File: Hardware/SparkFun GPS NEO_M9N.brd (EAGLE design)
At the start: 40.6 x 33.3 mm, 93 parts, among them J13 U.FL, J2 Qwiic Right Angle, J4 Qwiic Right Angle, U1 U-BLOX_NEO-M9N, U2 3.3V

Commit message: Initial issues dealt with, air wires etc
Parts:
- removed U$27: (no value), buzzard_labels (6):DSEL0
- removed U$32: (no value), buzzard_labels (5):JP32
- removed U$53: (no value), buzzard_labels (7):NEO#M8P3
- removed U$54: (no value), buzzard_labels (8):GPS#RTK1
- moved JP2 3.02 mm to (35.1, 11.9)
- moved JP1 1.90 mm to (35.1, 9.60)
- moved U$12 0.66 mm to (40.0, 9.50)
- moved D3 0.64 mm to (10.1, 24.4)
- moved U$25 0.54 mm to (39.8, 11.9)
- moved R8 0.53 mm to (4.09, 22.3)
- moved R9 0.41 mm to (9.55, 21.9)
- moved R10 0.36 mm to (11.4, 22.0)
- moved J3 0.33 mm to (10.1, 26.8)
- moved R7 0.31 mm to (2.59, 22.3)
- moved R12 0.30 mm to (7.52, 23.1)
- moved J2 0.28 mm to (5.08, 16.2)
- moved J4 0.28 mm to (35.6, 16.2)
- moved JP31 0.28 mm to (2.54, 30.5)
- moved JP41 0.28 mm to (38.1, 30.5)
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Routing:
- net 3.3V: track 115.8 -> 109.2 mm, vias 8 -> 7
- net N$1: track 0.00 -> 5.81 mm, vias 0 -> 1
- net N$5: track 0.67 -> 4.61 mm, vias 0 -> 1
- net N$8: track 0.67 -> 4.11 mm, vias 0 -> 1
- net N$12: track 52.7 -> 53.5 mm
- net GND: track 1.72 -> 2.56 mm, vias 159 -> 169
- net PPS: track 37.6 -> 36.8 mm
- net 5V: track 61.5 -> 60.7 mm
- net N$4: track 5.26 -> 5.88 mm
- net N$11: track 55.1 -> 55.6 mm
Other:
- board size 40.6 x 33.3 mm -> 40.6 x 33 mm

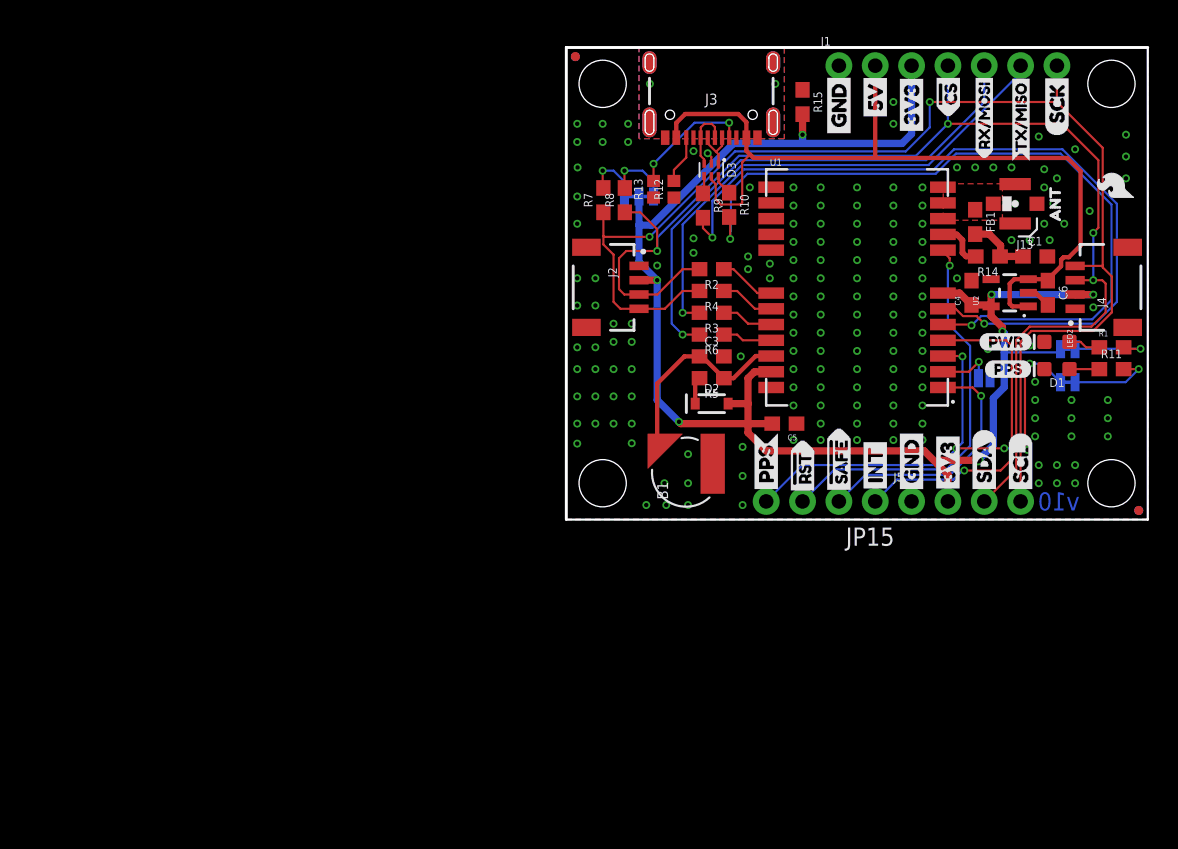
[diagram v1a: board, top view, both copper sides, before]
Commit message: Updates the order of the info boxes in the schematic, adds 10k pullup to D_SEL
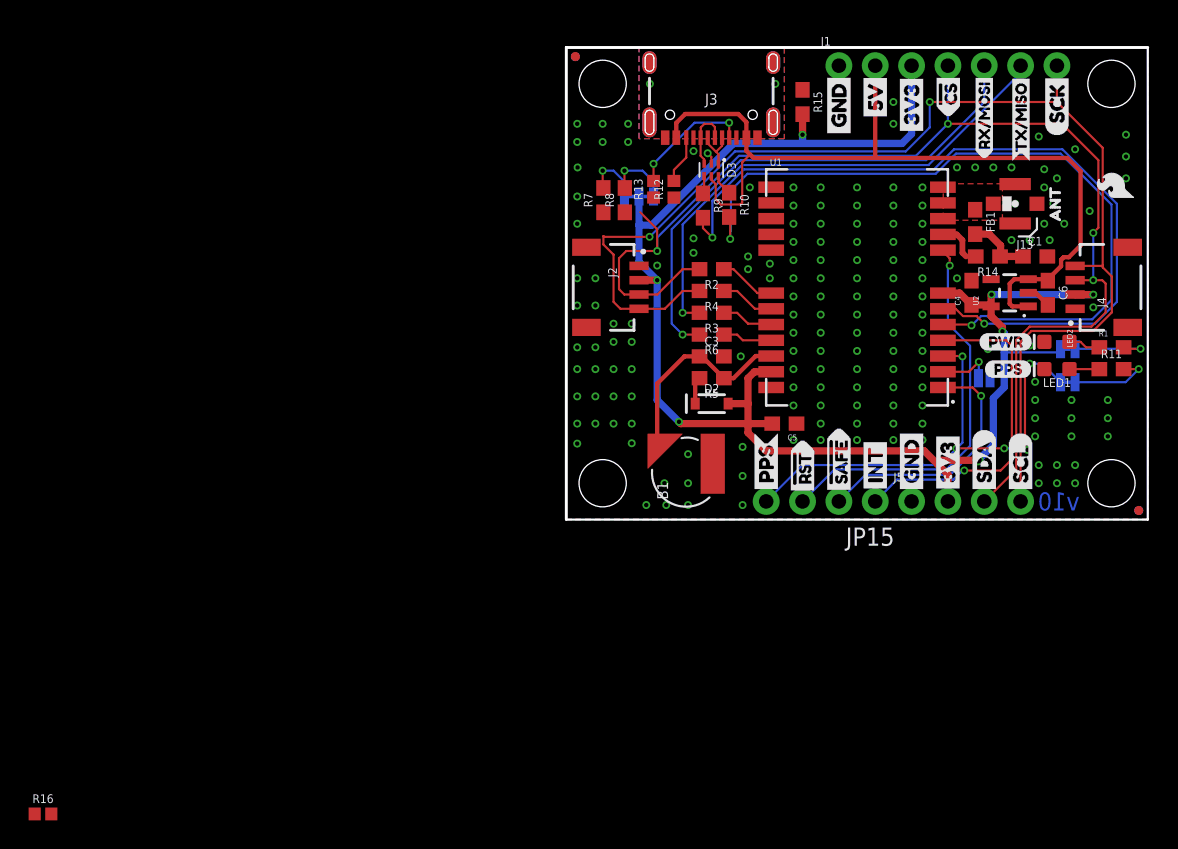
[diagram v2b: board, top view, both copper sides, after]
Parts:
- added R16: 10k, SparkFun-Resistors:0402
- moved LOGO2 6.28 mm to (20.2, 20.7)
- moved U$22 0.92 mm to (24.5, 18.4)
- renumbered D1 to LED1
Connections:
- net N$13 renamed VCC_RF
- net 3.3V: now also R16.2
- net D_SEL: now also R16.1
- net SCL/SCK: now also R8.1; no longer R7.1
- net SDA/!CS: now also R7.1; no longer R8.1
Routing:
- net SCL/SCK: track 89.1 -> 87.4 mm
- net SDA/!CS: track 88.0 -> 87.0 mm
- net VCC_RF: track 3.45 -> 2.78 mm
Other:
- board text added: "Elias Santistevan"
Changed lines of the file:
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@@
 <dimension x1="2.54" y1="2.54" x2="2.54" y2="30.48" x3="-2.54" y3="16.51" textsize="1.778" textratio="15" layer="47" unit="inch"/>
 <dimension x1="2.54" y1="30.48" x2="38.1" y2="30.48" x3="20.32" y3="45.72" textsize="1.778" textratio="15" layer="47" unit="inch"/>
+<text x="12.7" y="-17.78" size="1.778" layer="51" font="vector">Elias Santistevan</text>
 </plain>
 <attributes>
@@
 <attribute name="VALUE" x="5.08" y="21.4376" size="0.6096" layer="28" font="vector" ratio="20" rot="MR0" align="top-center"/>
 </element>
-<element name="D1" library="SparkFun-LED" package="LED-0603" value="Yellow" x="34.29" y="10.5156" smashed="yes" rot="R180">
+<element name="LED1" library="SparkFun-LED" package="LED-0603" value="Yellow" x="34.29" y="10.5156" smashed="yes" rot="R180">
 <attribute name="NAME" x="34.29" y="9.8806" size="0.6096" layer="25" font="vector" ratio="20" rot="R180" align="bottom-center"/>
 <attribute name="PROD_ID" value="DIO-09003" x="34.29" y="10.5156" size="1.778" layer="27" rot="R180" display="off"/>
@@
 <element name="U$15" library="buzzard_labels (5)" package="INT8" value="" x="21.59" y="1.651" smashed="yes" rot="R90"/>
 <element name="U$16" library="buzzard_labels (5)" package="INT8" value="" x="21.59" y="1.651" smashed="yes" rot="MR90"/>
-<element name="U$22" library="buzzard_labels (5)" package="U#BLOX3" value="" x="25.273" y="17.8816" smashed="yes" rot="MR0"/>
+<element name="U$22" library="buzzard_labels (5)" package="U#BLOX3" value="" x="24.511" y="18.3896" smashed="yes" rot="MR0"/>
 <element name="U$30" library="Labels" package="QWIIC-LOGO-MEDIUM" value="" x="4.191" y="8.4836" smashed="yes" rot="MR0"/>
 <element name="U$35" library="buzzard_labels (7)" package="#RST3" value="" x="16.51" y="1.397" smashed="yes" rot="R90"/>
@@
 <element name="U$34" library="buzzard_labels (36)" package="TX#MISO0" value="" x="31.7754" y="24.9936" smashed="yes" rot="R90"/>
 <element name="U$37" library="buzzard_labels (36)" package="TX#MISO1" value="" x="31.7754" y="24.0284" smashed="yes" rot="MR90"/>
-<element name="LOGO2" library="SparkFun-Aesthetics" package="SFE_LOGO_NAME_FLAME_.1" value="SFE_LOGO_NAME_FLAME.1_INCH" x="26.289" y="19.1516" smashed="yes" rot="MR0"/>
+<element name="LOGO2" library="SparkFun-Aesthetics" package="SFE_LOGO_NAME_FLAME_.1" value="SFE_LOGO_NAME_FLAME.1_INCH" x="20.193" y="20.6756" smashed="yes" rot="MR0"/>
 <element name="U1" library="gps" package="NEO-M9N" value="U-BLOX_NEO-M9N" x="20.32" y="16.2306" smashed="yes">
 <attribute name="NAME" x="14.22" y="24.7306" size="0.508" layer="25"/>
@@
 <attribute name="PROD_ID" value="RES-14340" x="6.096" y="23.0886" size="1.778" layer="27" font="vector" ratio="15" rot="R90" display="off"/>
 <attribute name="VALUE" x="6.858" y="23.0886" size="0.6096" layer="27" font="vector" ratio="20" rot="R90" align="top-center"/>
+</element>
+<element name="R16" library="SparkFun-Resistors" package="0402" value="10k" x="-36.576" y="-20.574" smashed="yes">
+<attribute name="NAME" x="-36.576" y="-19.812" size="0.6096" layer="25" font="vector" ratio="20" align="bottom-center"/>
+<attribute name="PROD_ID" value="RES-14241" x="-36.576" y="-20.574" size="1.778" layer="27" font="vector" display="off"/>
+<attribute name="VALUE" x="-36.576" y="-21.336" size="0.6096" layer="27" font="vector" ratio="20" align="top-center"/>
 </element>
 </elements>
@@
 <wire x1="5.97123125" y1="20.574" x2="5.08" y2="20.574" width="0.508" layer="16"/>
 <wire x1="11.68623125" y1="26.289" x2="5.97123125" y2="20.574" width="0.508" layer="16"/>
+<contactref element="R16" pad="2"/>
+<wire x1="6.35" y1="8.3566" x2="-35.996" y2="-20.574" width="0" layer="19" extent="1-16"/>
 </signal>
 <signal name="GND">
@@
 <contactref element="C3" pad="2"/>
 <contactref element="B1" pad="-"/>
-<contactref element="D1" pad="C"/>
+<contactref element="LED1" pad="C"/>
 <polygon width="0.1524" layer="1" isolate="0.2032" rank="4">
 <vertex x="0" y="32.9946"/>
@@
 <contactref element="J2" pad="4"/>
 <contactref element="J4" pad="4"/>
-<contactref element="R7" pad="1"/>
 <contactref element="R4" pad="2"/>
 <wire x1="5.08" y1="14.7306" x2="6.882" y2="14.7306" width="0.1524" layer="1"/>
@@
 <via x="5.8180875" y="19.7612" extent="1-16" drill="0.3048"/>
 <wire x1="2.5908" y1="19.2278" x2="3.302" y2="18.5166" width="0.1524" layer="1"/>
-<wire x1="2.5908" y1="21.4766" x2="2.5908" y2="19.812" width="0.1524" layer="1"/>
 <wire x1="2.5908" y1="19.812" x2="2.5908" y2="19.2278" width="0.1524" layer="1"/>
 <wire x1="5.8180875" y1="19.7612" x2="2.6416" y2="19.7612" width="0.1524" layer="1"/>
 <wire x1="2.6416" y1="19.7612" x2="2.5908" y2="19.812" width="0.1524" layer="1"/>
+<contactref element="R8" pad="1"/>
+<wire x1="2.6416" y1="19.7612" x2="4.0894" y2="21.4766" width="0" layer="19" extent="1-1"/>
 </signal>
 <signal name="SDA/!CS">
 <contactref element="J2" pad="3"/>
 <contactref element="J4" pad="3"/>
-<contactref element="R8" pad="1"/>
 <contactref element="R2" pad="2"/>
 <wire x1="6.358" y1="15.7306" x2="8.128" y2="17.5006" width="0.1524" layer="1"/>
@@
 <contactref element="J5" pad="3"/>
 <wire x1="31.4452" y1="3.5052" x2="29.21" y2="1.27" width="0.1524" layer="1"/>
-<wire x1="4.0894" y1="21.4766" x2="5.168" y2="21.4766" width="0.1524" layer="1"/>
 <wire x1="5.168" y1="21.4766" x2="6.35" y2="20.2946" width="0.1524" layer="1"/>
 <wire x1="6.35" y1="20.2946" x2="6.35" y2="18.7706" width="0.1524" layer="1"/>
@@
 <wire x1="4.056" y1="15.7306" x2="3.683" y2="16.1036" width="0.1524" layer="1"/>
 <wire x1="5.08" y1="15.7306" x2="6.358" y2="15.7306" width="0.1524" layer="1"/>
+<contactref element="R7" pad="1"/>
+<wire x1="5.168" y1="21.4766" x2="2.5908" y2="21.4766" width="0" layer="19" extent="1-1"/>
 </signal>
 <signal name="!RESET">
@@
 </signal>
 <signal name="N$2">
-<contactref element="D1" pad="A"/>
+<contactref element="LED1" pad="A"/>
 <contactref element="R11" pad="1"/>
 <wire x1="35.167" y1="10.5156" x2="37.25" y2="10.5156" width="0.1524" layer="1"/>
@@
 <contactref element="FB1" pad="1"/>
 <contactref element="U1" pad="11"/>
+<wire x1="28.575" y1="21.6526" x2="29.844" y2="22.0726" width="0" layer="19" extent="1-1"/>
+<wire x1="26.32" y1="22.1306" x2="28.575" y2="21.6526" width="0" layer="19" extent="1-1"/>
 </signal>
 <signal name="N$10">
@@
 </signal>
 <signal name="D_SEL">
-<contactref element="JP4" pad="2"/>
 <wire x1="28.136" y1="10.3306" x2="28.829" y2="11.0236" width="0.1524" layer="1"/>
 <via x="28.829" y="11.0236" extent="1-16" drill="0.3048"/>
 <wire x1="28.829" y1="11.0236" x2="28.829" y2="9.906" width="0.1524" layer="16"/>
-<wire x1="28.8036" y1="9.8806" x2="28.829" y2="9.906" width="0.1524" layer="16"/>
 <contactref element="U1" pad="2"/>
 <wire x1="26.32" y1="10.3306" x2="28.136" y2="10.3306" width="0.1524" layer="1"/>
-</signal>
-<signal name="N$13">
-<contactref element="R14" pad="2"/>
+<contactref element="R16" pad="1"/>
+<contactref element="JP4" pad="2"/>
+<wire x1="26.32" y1="10.3306" x2="-37.156" y2="-20.574" width="0" layer="19" extent="1-1"/>
+<wire x1="28.8036" y1="9.8806" x2="28.829" y2="9.906" width="0" layer="19" extent="16-16"/>
+</signal>
+<signal name="VCC_RF">
 <wire x1="27.686" y1="18.6436" x2="27.686" y2="19.5326" width="0.4064" layer="1"/>
 <wire x1="27.686" y1="18.6436" x2="27.94" y2="18.3896" width="0.4064" layer="1"/>
-<wire x1="27.94" y1="18.3896" x2="28.614" y2="18.3896" width="0.4064" layer="1"/>
 <contactref element="U1" pad="9"/>
 <wire x1="27.686" y1="19.5326" x2="27.288" y2="19.9306" width="0.4064" layer="1"/>
 <wire x1="27.288" y1="19.9306" x2="26.32" y2="19.9306" width="0.4064" layer="1"/>
+<contactref element="R14" pad="2"/>
+<wire x1="27.94" y1="18.3896" x2="28.614" y2="18.3896" width="0" layer="19" extent="1-1"/>
 </signal>
 <signal name="ANT_VCC">

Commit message: Routes 10k pullup resistor, adds labels, fixes air wires
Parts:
- added U$11: (no value), board lables:SPI1
- added U$13: (no value), SparkFun-Aesthetics:QWIIC_4MM
- added U$2: (no value), board lables:NEO#M9N1
- moved R16 73.2 mm to (29.7, 10.4), turned to 270 degrees
- moved U$12 2.55 mm to (39.8, 12.0)
- moved U$25 2.29 mm to (39.8, 9.58)
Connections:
- net SCL/SCK: now also R7.1; no longer R8.1
- net SDA/!CS: now also R8.1; no longer R7.1
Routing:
- net 3.3V: track 109.2 -> 110.6 mm, vias 7 -> 8
- net SDA/!CS: track 87.0 -> 88.0 mm
- net SCL/SCK: track 87.4 -> 88.4 mm
- net D_SEL: track 3.91 -> 4.81 mm
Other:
- board text added: "v01"
- board text removed: "v10"
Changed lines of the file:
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@@
 <layer number="37" name="tTest" color="7" fill="1" visible="no" active="yes"/>
 <layer number="38" name="bTest" color="7" fill="1" visible="no" active="yes"/>
-<layer number="39" name="tKeepout" color="4" fill="11" visible="yes" active="yes"/>
+<layer number="39" name="tKeepout" color="4" fill="11" visible="no" active="yes"/>
 <layer number="40" name="bKeepout" color="1" fill="11" visible="no" active="yes"/>
 <layer number="41" name="tRestrict" color="4" fill="10" visible="no" active="yes"/>
@@
 <wire x1="40.64" y1="32.9946" x2="40.64" y2="0" width="0.1524" layer="20"/>
 <wire x1="40.64" y1="0" x2="0" y2="0" width="0.1524" layer="20"/>
-<text x="34.417" y="1.27" size="1.27" layer="16" font="vector" ratio="15" rot="MR180" align="center">v10</text>
+<text x="34.417" y="1.27" size="1.27" layer="16" font="vector" ratio="15" rot="MR180" align="center">v01</text>
 <text x="-2.54" y="-8.89" size="1.778" layer="47">Measurements in inches</text>
 <dimension x1="0" y1="0" x2="0" y2="33.02" x3="-7.62" y3="16.51" textsize="1.778" textratio="15" layer="47" unit="inch"/>
@@
 <attribute name="PROD_ID" value="CONN-09696" x="21.59" y="1.27" size="1.778" layer="27" font="vector" ratio="15" rot="R180" display="off"/>
 </element>
-<element name="U$12" library="buzzard_labels" package="JP20" value="" x="40.005" y="9.4996" smashed="yes" rot="MR0"/>
+<element name="U$12" library="buzzard_labels" package="JP20" value="" x="39.751" y="12.0396" smashed="yes" rot="MR0"/>
 <element name="U$60" library="Labels" package="3V3-04" value="" x="24.13" y="26.6446" smashed="yes" rot="MR90"/>
 <element name="U$61" library="Labels" package="3V3-04" value="" x="24.13" y="26.6446" smashed="yes" rot="R90"/>
 <element name="U$62" library="Labels" package="GND-04" value="" x="19.05" y="26.5176" smashed="yes" rot="MR90"/>
 <element name="U$63" library="Labels" package="GND-04" value="" x="19.05" y="26.5176" smashed="yes" rot="R90"/>
-<element name="U$25" library="buzzard_labels (5)" package="JP10" value="" x="39.8018" y="11.8618" smashed="yes" rot="MR0"/>
+<element name="U$25" library="buzzard_labels (5)" package="JP10" value="" x="39.8018" y="9.5758" smashed="yes" rot="MR0"/>
 <element name="U$55" library="buzzard_labels (9)" package="ANT0" value="" x="34.163" y="20.1676" smashed="yes" rot="R90"/>
 <element name="U$18" library="Labels" package="PWR-()-03" value="" x="28.829" y="12.4206" smashed="yes"/>
@@
 <attribute name="VALUE" x="6.858" y="23.0886" size="0.6096" layer="27" font="vector" ratio="20" rot="R90" align="top-center"/>
 </element>
-<element name="R16" library="SparkFun-Resistors" package="0402" value="10k" x="-36.576" y="-20.574" smashed="yes">
-<attribute name="NAME" x="-36.576" y="-19.812" size="0.6096" layer="25" font="vector" ratio="20" align="bottom-center"/>
-<attribute name="PROD_ID" value="RES-14241" x="-36.576" y="-20.574" size="1.778" layer="27" font="vector" display="off"/>
-<attribute name="VALUE" x="-36.576" y="-21.336" size="0.6096" layer="27" font="vector" ratio="20" align="top-center"/>
-</element>
+<element name="R16" library="SparkFun-Resistors" package="0402" value="10k" x="29.718" y="10.414" smashed="yes" rot="R270">
+<attribute name="NAME" x="30.48" y="10.414" size="0.6096" layer="25" font="vector" ratio="20" rot="R270" align="bottom-center"/>
+<attribute name="PROD_ID" value="RES-14241" x="29.718" y="10.414" size="1.778" layer="27" font="vector" rot="R270" display="off"/>
+<attribute name="VALUE" x="28.956" y="10.414" size="0.6096" layer="27" font="vector" ratio="20" rot="R270" align="top-center"/>
+</element>
+<element name="U$2" library="board lables" package="NEO#M9N1" value="" x="27.686" y="16.002" smashed="yes" rot="MR0"/>
+<element name="U$11" library="board lables" package="SPI1" value="" x="30.734" y="7.62" smashed="yes" rot="MR0"/>
+<element name="U$13" library="SparkFun-Aesthetics" package="QWIIC_4MM" value="" x="38.354" y="20.574" smashed="yes"/>
 </elements>
 <signals>
@@
 <wire x1="35.568" y1="15.7226" x2="36.83" y2="15.7226" width="0.508" layer="1"/>
 <wire x1="29.845" y1="8.4836" x2="30.607" y2="9.245603125" width="0.508" layer="16"/>
+<via x="30.48" y="13.1572" extent="1-16" drill="0.3048"/>
 <wire x1="30.607" y1="9.245603125" x2="30.607" y2="11.684" width="0.508" layer="16"/>
-<via x="30.48" y="13.1572" extent="1-16" drill="0.3048"/>
 <wire x1="30.48" y1="13.1572" x2="30.48" y2="13.4366" width="0.508" layer="1"/>
 <wire x1="25.019" y1="4.8006" x2="25.9588" y2="3.8608" width="0.508" layer="1"/>
@@
 <wire x1="11.68623125" y1="26.289" x2="5.97123125" y2="20.574" width="0.508" layer="16"/>
 <contactref element="R16" pad="2"/>
-<wire x1="6.35" y1="8.3566" x2="-35.996" y2="-20.574" width="0" layer="19" extent="1-16"/>
+<wire x1="29.718" y1="9.834" x2="29.845" y2="9.707" width="0.508" layer="1"/>
+<wire x1="29.845" y1="9.707" x2="29.845" y2="8.4836" width="0.508" layer="1"/>
+<via x="29.845" y="8.4836" extent="1-16" drill="0.3048"/>
 </signal>
 <signal name="GND">
@@
 <contactref element="J5" pad="4"/>
 <wire x1="31.75" y1="1.27" x2="31.75" y2="12.4206" width="0.1524" layer="1"/>
-<wire x1="3.302" y1="18.5166" x2="3.302" y2="15.2146" width="0.1524" layer="1"/>
 <via x="5.8180875" y="19.7612" extent="1-16" drill="0.3048"/>
-<wire x1="2.5908" y1="19.2278" x2="3.302" y2="18.5166" width="0.1524" layer="1"/>
-<wire x1="2.5908" y1="19.812" x2="2.5908" y2="19.2278" width="0.1524" layer="1"/>
-<wire x1="5.8180875" y1="19.7612" x2="2.6416" y2="19.7612" width="0.1524" layer="1"/>
-<wire x1="2.6416" y1="19.7612" x2="2.5908" y2="19.812" width="0.1524" layer="1"/>
-<contactref element="R8" pad="1"/>
-<wire x1="2.6416" y1="19.7612" x2="4.0894" y2="21.4766" width="0" layer="19" extent="1-1"/>
+<contactref element="R7" pad="1"/>
+<wire x1="3.302" y1="20.7654" x2="2.5908" y2="21.4766" width="0.1524" layer="1"/>
+<wire x1="3.302" y1="15.2146" x2="3.302" y2="19.812" width="0.1524" layer="1"/>
+<wire x1="3.302" y1="19.812" x2="3.302" y2="20.7654" width="0.1524" layer="1"/>
+<wire x1="3.302" y1="19.812" x2="5.7672875" y2="19.812" width="0.1524" layer="1"/>
+<wire x1="5.7672875" y1="19.812" x2="5.8180875" y2="19.7612" width="0.1524" layer="1"/>
 </signal>
 <signal name="SDA/!CS">
@@
 <contactref element="J5" pad="3"/>
 <wire x1="31.4452" y1="3.5052" x2="29.21" y2="1.27" width="0.1524" layer="1"/>
-<wire x1="5.168" y1="21.4766" x2="6.35" y2="20.2946" width="0.1524" layer="1"/>
+<wire x1="6.35" y1="20.2946" x2="5.168" y2="21.4766" width="0.1524" layer="1"/>
 <wire x1="6.35" y1="20.2946" x2="6.35" y2="18.7706" width="0.1524" layer="1"/>
 <wire x1="37.69396875" y1="16.493628125" x2="37.69396875" y2="14.477625" width="0.1524" layer="1"/>
@@
 <wire x1="4.056" y1="15.7306" x2="3.683" y2="16.1036" width="0.1524" layer="1"/>
 <wire x1="5.08" y1="15.7306" x2="6.358" y2="15.7306" width="0.1524" layer="1"/>
-<contactref element="R7" pad="1"/>
-<wire x1="5.168" y1="21.4766" x2="2.5908" y2="21.4766" width="0" layer="19" extent="1-1"/>
+<contactref element="R8" pad="1"/>
+<wire x1="5.168" y1="21.4766" x2="4.0894" y2="21.4766" width="0.1524" layer="1"/>
 </signal>
 <signal name="!RESET">
@@
 <contactref element="FB1" pad="1"/>
 <contactref element="U1" pad="11"/>
-<wire x1="28.575" y1="21.6526" x2="29.844" y2="22.0726" width="0" layer="19" extent="1-1"/>
-<wire x1="26.32" y1="22.1306" x2="28.575" y2="21.6526" width="0" layer="19" extent="1-1"/>
 </signal>
 <signal name="N$10">
@@
 <contactref element="R16" pad="1"/>
 <contactref element="JP4" pad="2"/>
-<wire x1="26.32" y1="10.3306" x2="-37.156" y2="-20.574" width="0" layer="19" extent="1-1"/>
+<wire x1="29.6884" y1="11.0236" x2="29.718" y2="10.994" width="0.254" layer="1"/>
+<wire x1="28.829" y1="11.0236" x2="29.6884" y2="11.0236" width="0.1524" layer="1"/>
 <wire x1="28.8036" y1="9.8806" x2="28.829" y2="9.906" width="0" layer="19" extent="16-16"/>
 </signal>
